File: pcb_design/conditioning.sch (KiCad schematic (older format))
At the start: 41 parts, among them U3 OPA2376AID, U4 LM2903-SO8

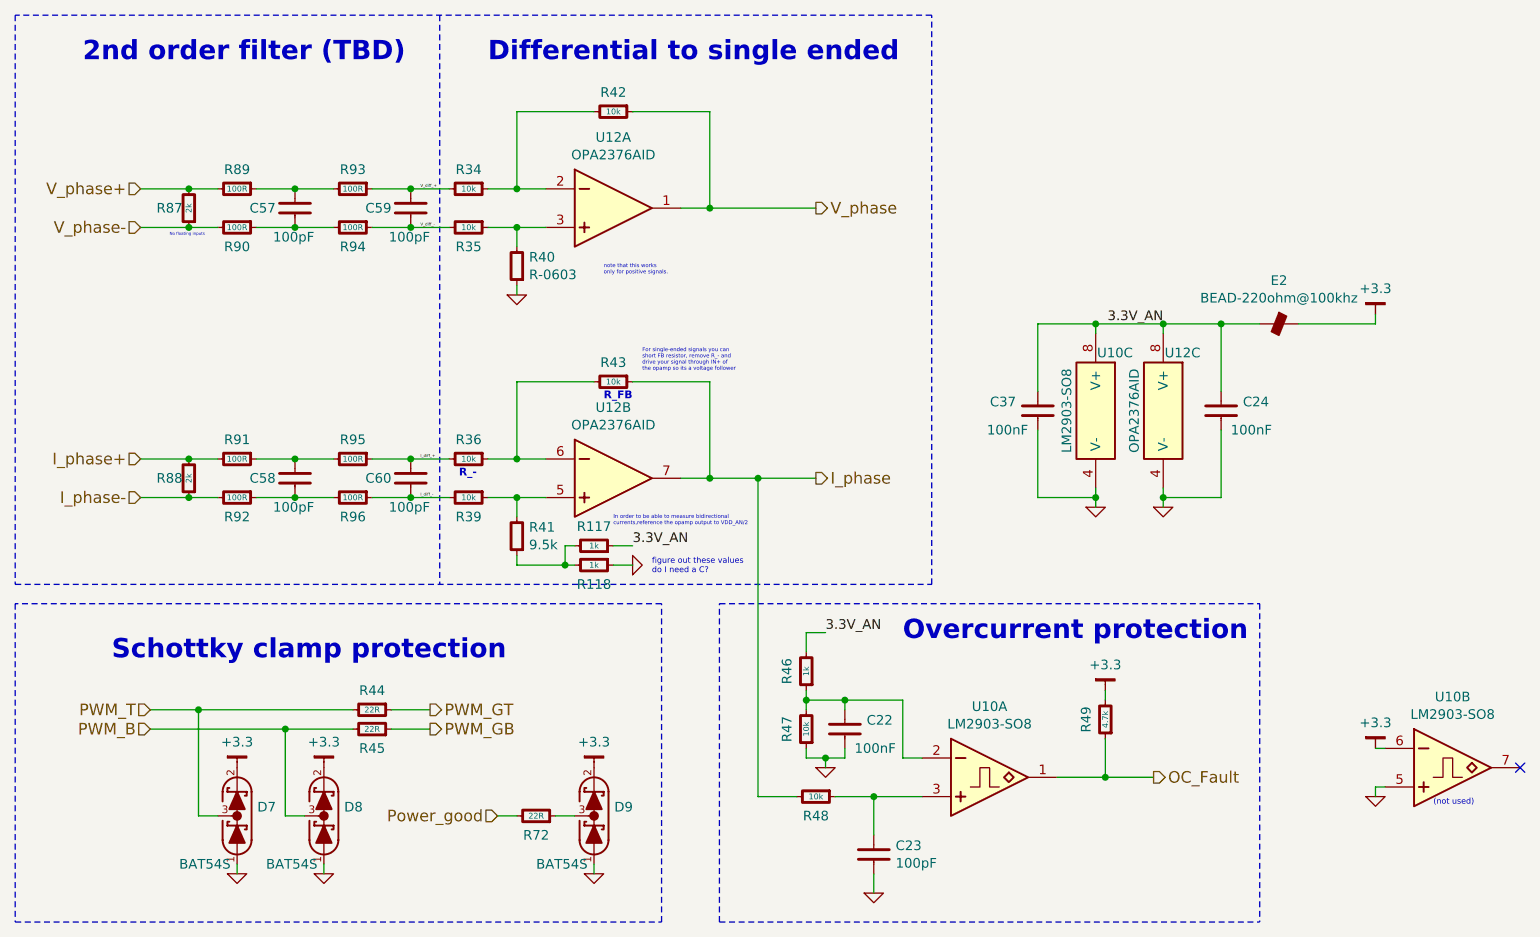
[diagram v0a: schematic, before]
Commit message: Added reverse polarity protection on the isolated side of CON connector. Also, more layout
Signed-off-by: Marcos Chaparro <mchaparro@paltatech.com>
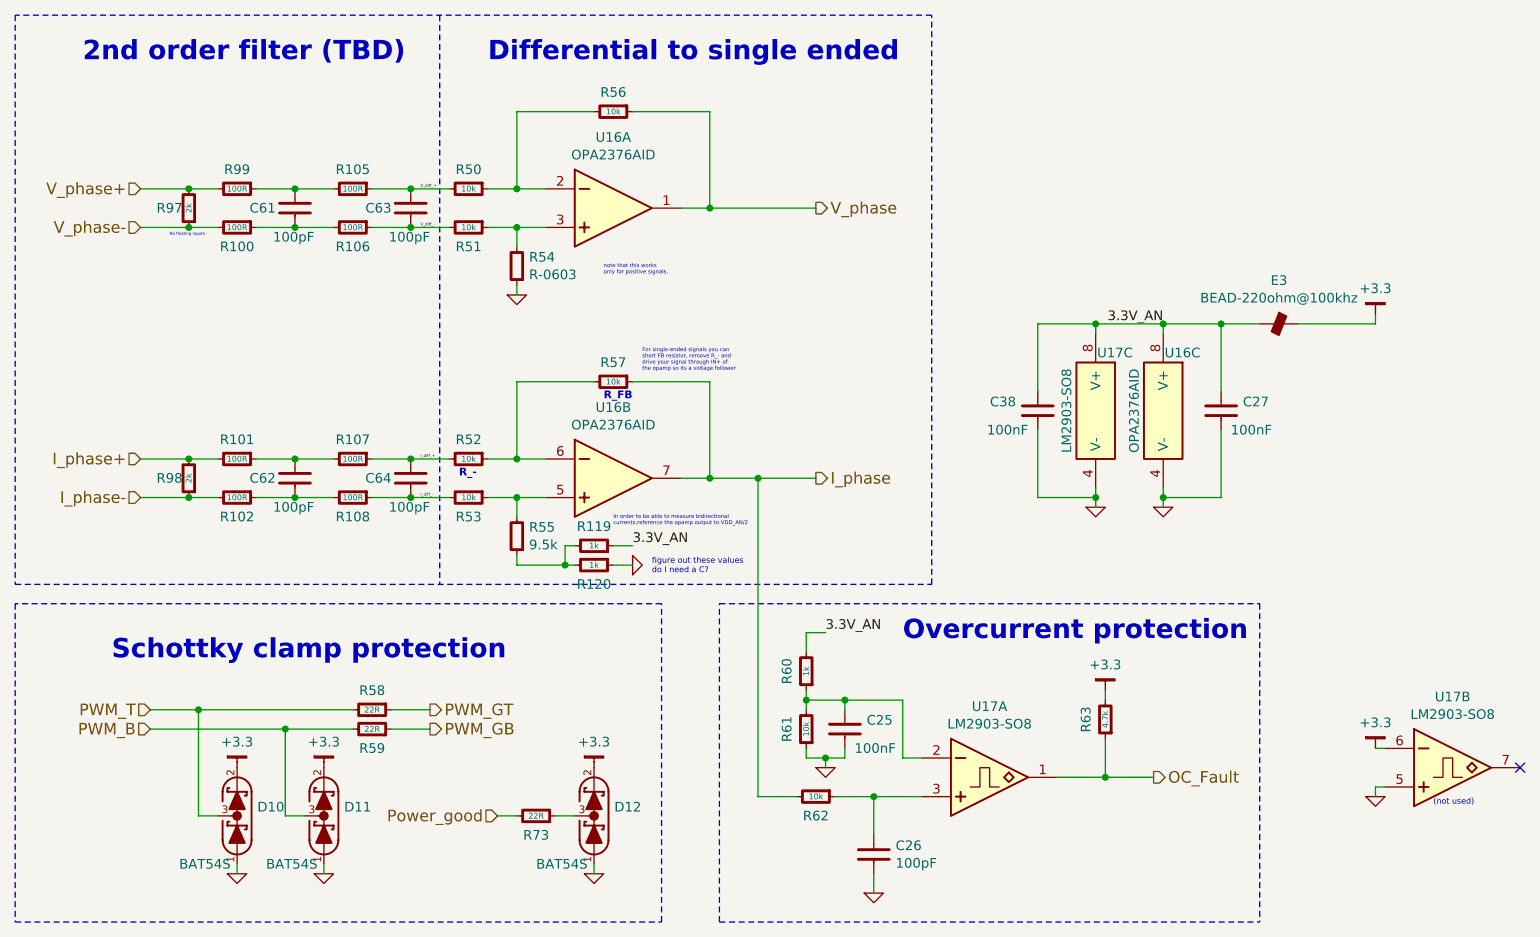
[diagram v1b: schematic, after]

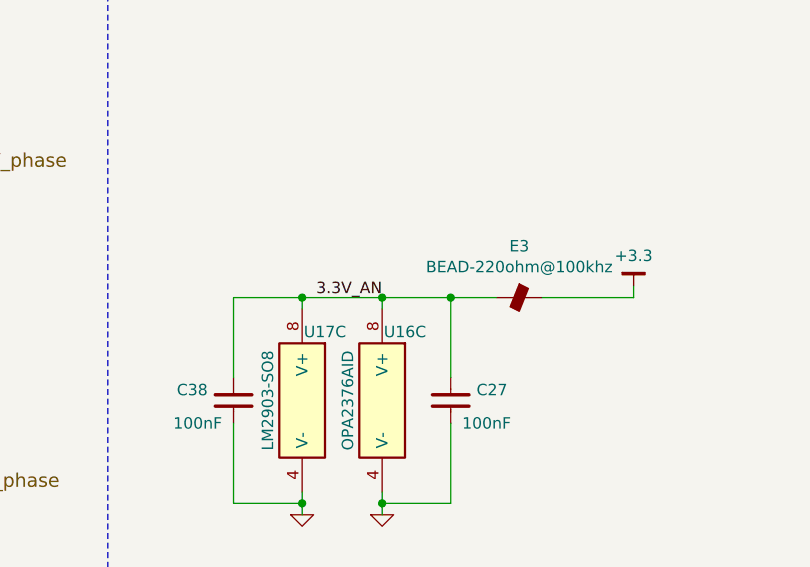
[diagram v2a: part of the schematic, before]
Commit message: Routing complete. Added 3D models. No DRC errors, a few ERC warnings
Signed-off-by: Marcos Chaparro <mchaparro@paltatech.com>
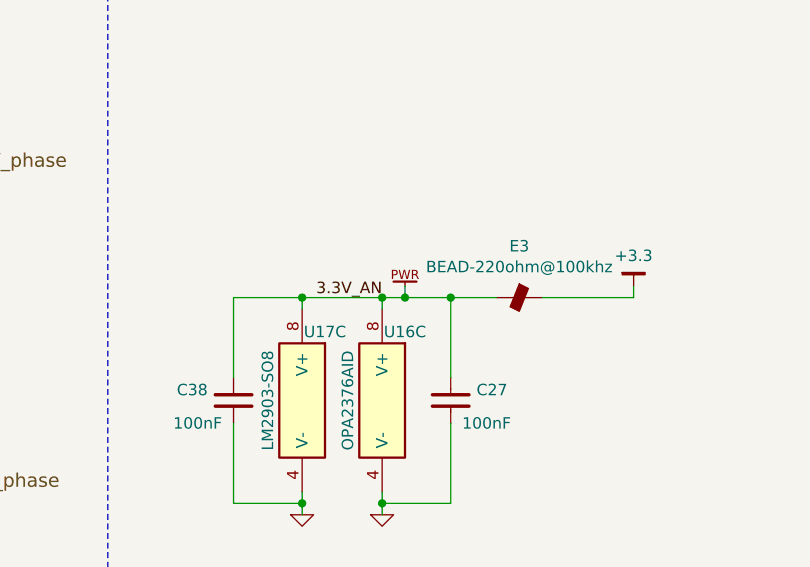
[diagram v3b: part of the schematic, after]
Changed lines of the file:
@@
 $EndComp
 $Comp
-L GND #PWR051
+L GND #PWR056
 U 1 1 588D9158
 P 5100 3000
-AR Path="/5886DA84/588D9158" Ref="#PWR051"  Part="1"
-AR Path="/588C2790/588D9158" Ref="#PWR0113"  Part="1"
-AR Path="/588C4E84/588D9158" Ref="#PWR0129"  Part="1"
-F 0 "#PWR0129" H 5100 3000 30  0001 C CNN
+AR Path="/5886DA84/588D9158" Ref="#PWR056"  Part="1"
+AR Path="/588C2790/588D9158" Ref="#PWR0125"  Part="1"
+AR Path="/588C4E84/588D9158" Ref="#PWR0142"  Part="1"
+F 0 "#PWR0142" H 5100 3000 30  0001 C CNN
 F 1 "GND" H 5100 2930 30  0001 C CNN
 F 2 "" H 5100 3000 60  0000 C CNN
@@
 $EndComp
 $Comp
-L GND #PWR052
+L GND #PWR057
 U 1 1 588D96F7
 P 5700 4400
-AR Path="/5886DA84/588D96F7" Ref="#PWR052"  Part="1"
-AR Path="/588C2790/588D96F7" Ref="#PWR0114"  Part="1"
-AR Path="/588C4E84/588D96F7" Ref="#PWR0130"  Part="1"
-F 0 "#PWR0130" H 5700 4400 30  0001 C CNN
+AR Path="/5886DA84/588D96F7" Ref="#PWR057"  Part="1"
+AR Path="/588C2790/588D96F7" Ref="#PWR0126"  Part="1"
+AR Path="/588C4E84/588D96F7" Ref="#PWR0143"  Part="1"
+F 0 "#PWR0143" H 5700 4400 30  0001 C CNN
 F 1 "GND" H 5700 4330 30  0001 C CNN
 F 2 "" H 5700 4400 60  0000 C CNN
@@
 $EndComp
 $Comp
-L GND #PWR053
+L GND #PWR058
 U 1 1 588DAB09
 P 6950 6100
-AR Path="/5886DA84/588DAB09" Ref="#PWR053"  Part="1"
-AR Path="/588C2790/588DAB09" Ref="#PWR0115"  Part="1"
-AR Path="/588C4E84/588DAB09" Ref="#PWR0131"  Part="1"
-F 0 "#PWR0131" H 6950 6100 30  0001 C CNN
+AR Path="/5886DA84/588DAB09" Ref="#PWR058"  Part="1"
+AR Path="/588C2790/588DAB09" Ref="#PWR0127"  Part="1"
+AR Path="/588C4E84/588DAB09" Ref="#PWR0144"  Part="1"
+F 0 "#PWR0144" H 6950 6100 30  0001 C CNN
 F 1 "GND" H 6950 6030 30  0001 C CNN
 F 2 "" H 6950 6100 60  0000 C CNN
@@
 $EndComp
 $Comp
-L GND #PWR054
+L GND #PWR059
 U 1 1 588DB3CB
 P 6700 5450
-AR Path="/5886DA84/588DB3CB" Ref="#PWR054"  Part="1"
-AR Path="/588C2790/588DB3CB" Ref="#PWR0116"  Part="1"
-AR Path="/588C4E84/588DB3CB" Ref="#PWR0132"  Part="1"
-F 0 "#PWR0132" H 6700 5450 30  0001 C CNN
+AR Path="/5886DA84/588DB3CB" Ref="#PWR059"  Part="1"
+AR Path="/588C2790/588DB3CB" Ref="#PWR0128"  Part="1"
+AR Path="/588C4E84/588DB3CB" Ref="#PWR0145"  Part="1"
+F 0 "#PWR0145" H 6700 5450 30  0001 C CNN
 F 1 "GND" H 6700 5380 30  0001 C CNN
 F 2 "" H 6700 5450 60  0000 C CNN
@@
 $EndComp
 $Comp
-L GND #PWR055
+L GND #PWR060
 U 1 1 588818FC
 P 8450 4100
-AR Path="/5886DA84/588818FC" Ref="#PWR055"  Part="1"
-AR Path="/588C2790/588818FC" Ref="#PWR0117"  Part="1"
-AR Path="/588C4E84/588818FC" Ref="#PWR0133"  Part="1"
-F 0 "#PWR0133" H 8450 4100 30  0001 C CNN
+AR Path="/5886DA84/588818FC" Ref="#PWR060"  Part="1"
+AR Path="/588C2790/588818FC" Ref="#PWR0129"  Part="1"
+AR Path="/588C4E84/588818FC" Ref="#PWR0146"  Part="1"
+F 0 "#PWR0146" H 8450 4100 30  0001 C CNN
 F 1 "GND" H 8450 4030 30  0001 C CNN
 F 2 "" H 8450 4100 60  0000 C CNN
@@
 $EndComp
 $Comp
-L GND #PWR056
+L GND #PWR061
 U 1 1 58891279
 P 3650 6000
-AR Path="/5886DA84/58891279" Ref="#PWR056"  Part="1"
-AR Path="/588C2790/58891279" Ref="#PWR0118"  Part="1"
-AR Path="/588C4E84/58891279" Ref="#PWR0134"  Part="1"
-F 0 "#PWR0134" H 3650 6000 30  0001 C CNN
+AR Path="/5886DA84/58891279" Ref="#PWR061"  Part="1"
+AR Path="/588C2790/58891279" Ref="#PWR0130"  Part="1"
+AR Path="/588C4E84/58891279" Ref="#PWR0147"  Part="1"
+F 0 "#PWR0147" H 3650 6000 30  0001 C CNN
 F 1 "GND" H 3650 5930 30  0001 C CNN
 F 2 "" H 3650 6000 60  0000 C CNN
@@
 $EndComp
 $Comp
-L GND #PWR057
+L GND #PWR062
 U 1 1 58891376
 P 4100 6000
-AR Path="/5886DA84/58891376" Ref="#PWR057"  Part="1"
-AR Path="/588C2790/58891376" Ref="#PWR0119"  Part="1"
-AR Path="/588C4E84/58891376" Ref="#PWR0135"  Part="1"
-F 0 "#PWR0135" H 4100 6000 30  0001 C CNN
+AR Path="/5886DA84/58891376" Ref="#PWR062"  Part="1"
+AR Path="/588C2790/58891376" Ref="#PWR0131"  Part="1"
+AR Path="/588C4E84/58891376" Ref="#PWR0148"  Part="1"
+F 0 "#PWR0148" H 4100 6000 30  0001 C CNN
 F 1 "GND" H 4100 5930 30  0001 C CNN
 F 2 "" H 4100 6000 60  0000 C CNN
@@
 $EndComp
 $Comp
-L GND #PWR058
+L GND #PWR063
 U 1 1 5889172A
 P 5500 6000
-AR Path="/5886DA84/5889172A" Ref="#PWR058"  Part="1"
-AR Path="/588C2790/5889172A" Ref="#PWR0120"  Part="1"
-AR Path="/588C4E84/5889172A" Ref="#PWR0136"  Part="1"
-F 0 "#PWR0136" H 5500 6000 30  0001 C CNN
+AR Path="/5886DA84/5889172A" Ref="#PWR063"  Part="1"
+AR Path="/588C2790/5889172A" Ref="#PWR0132"  Part="1"
+AR Path="/588C4E84/5889172A" Ref="#PWR0149"  Part="1"
+F 0 "#PWR0149" H 5500 6000 30  0001 C CNN
 F 1 "GND" H 5500 5930 30  0001 C CNN
 F 2 "" H 5500 6000 60  0000 C CNN
@@
 $EndComp
 $Comp
-L GND #PWR059
+L GND #PWR064
 U 1 1 58899625
 P 8100 4100
-AR Path="/5886DA84/58899625" Ref="#PWR059"  Part="1"
-AR Path="/588C2790/58899625" Ref="#PWR0121"  Part="1"
-AR Path="/588C4E84/58899625" Ref="#PWR0137"  Part="1"
-F 0 "#PWR0137" H 8100 4100 30  0001 C CNN
+AR Path="/5886DA84/58899625" Ref="#PWR064"  Part="1"
+AR Path="/588C2790/58899625" Ref="#PWR0133"  Part="1"
+AR Path="/588C4E84/58899625" Ref="#PWR0150"  Part="1"
+F 0 "#PWR0150" H 8100 4100 30  0001 C CNN
 F 1 "GND" H 8100 4030 30  0001 C CNN
 F 2 "" H 8100 4100 60  0000 C CNN
@@
 2nd order filter (TBD)
 $Comp
-L +3.3 #PWR060
+L +3.3 #PWR065
 U 1 1 588B58C9
 P 9550 3100
-AR Path="/5886DA84/588B58C9" Ref="#PWR060"  Part="1"
-AR Path="/588C2790/588B58C9" Ref="#PWR0122"  Part="1"
-AR Path="/588C4E84/588B58C9" Ref="#PWR0138"  Part="1"
-F 0 "#PWR0138" H 9600 3150 30  0001 C CNN
+AR Path="/5886DA84/588B58C9" Ref="#PWR065"  Part="1"
+AR Path="/588C2790/588B58C9" Ref="#PWR0134"  Part="1"
+AR Path="/588C4E84/588B58C9" Ref="#PWR0151"  Part="1"
+F 0 "#PWR0151" H 9600 3150 30  0001 C CNN
 F 1 "+3.3" H 9550 3233 50  0000 C CNN
 F 2 "" H 300 -50 60  0000 C CNN
@@
 $EndComp
 $Comp
-L +3.3 #PWR061
+L +3.3 #PWR066
 U 1 1 588B5AA1
 P 8150 5050
-AR Path="/5886DA84/588B5AA1" Ref="#PWR061"  Part="1"
-AR Path="/588C2790/588B5AA1" Ref="#PWR0123"  Part="1"
-AR Path="/588C4E84/588B5AA1" Ref="#PWR0139"  Part="1"
-F 0 "#PWR0139" H 8200 5100 30  0001 C CNN
+AR Path="/5886DA84/588B5AA1" Ref="#PWR066"  Part="1"
+AR Path="/588C2790/588B5AA1" Ref="#PWR0135"  Part="1"
+AR Path="/588C4E84/588B5AA1" Ref="#PWR0152"  Part="1"
+F 0 "#PWR0152" H 8200 5100 30  0001 C CNN
 F 1 "+3.3" H 8150 5183 50  0000 C CNN
 F 2 "" H 300 -50 60  0000 C CNN
@@
 $EndComp
 $Comp
-L +3.3 #PWR062
+L +3.3 #PWR067
 U 1 1 588B5C24
 P 5500 5450
-AR Path="/5886DA84/588B5C24" Ref="#PWR062"  Part="1"
-AR Path="/588C2790/588B5C24" Ref="#PWR0124"  Part="1"
-AR Path="/588C4E84/588B5C24" Ref="#PWR0140"  Part="1"
-F 0 "#PWR0140" H 5550 5500 30  0001 C CNN
+AR Path="/5886DA84/588B5C24" Ref="#PWR067"  Part="1"
+AR Path="/588C2790/588B5C24" Ref="#PWR0136"  Part="1"
+AR Path="/588C4E84/588B5C24" Ref="#PWR0153"  Part="1"
+F 0 "#PWR0153" H 5550 5500 30  0001 C CNN
 F 1 "+3.3" H 5500 5583 50  0000 C CNN
 F 2 "" H -2350 350 60  0000 C CNN
@@
 $EndComp
 $Comp
-L +3.3 #PWR063
+L +3.3 #PWR068
 U 1 1 588B5D7A
 P 3650 5450
-AR Path="/5886DA84/588B5D7A" Ref="#PWR063"  Part="1"
-AR Path="/588C2790/588B5D7A" Ref="#PWR0125"  Part="1"
-AR Path="/588C4E84/588B5D7A" Ref="#PWR0141"  Part="1"
-F 0 "#PWR0141" H 3700 5500 30  0001 C CNN
+AR Path="/5886DA84/588B5D7A" Ref="#PWR068"  Part="1"
+AR Path="/588C2790/588B5D7A" Ref="#PWR0137"  Part="1"
+AR Path="/588C4E84/588B5D7A" Ref="#PWR0154"  Part="1"
+F 0 "#PWR0154" H 3700 5500 30  0001 C CNN
 F 1 "+3.3" H 3650 5583 50  0000 C CNN
 F 2 "" H -4200 350 60  0000 C CNN
@@
 $EndComp
 $Comp
-L +3.3 #PWR064
+L +3.3 #PWR069
 U 1 1 588B5E7B
 P 4100 5450
-AR Path="/5886DA84/588B5E7B" Ref="#PWR064"  Part="1"
-AR Path="/588C2790/588B5E7B" Ref="#PWR0126"  Part="1"
-AR Path="/588C4E84/588B5E7B" Ref="#PWR0142"  Part="1"
-F 0 "#PWR0142" H 4150 5500 30  0001 C CNN
+AR Path="/5886DA84/588B5E7B" Ref="#PWR069"  Part="1"
+AR Path="/588C2790/588B5E7B" Ref="#PWR0138"  Part="1"
+AR Path="/588C4E84/588B5E7B" Ref="#PWR0155"  Part="1"
+F 0 "#PWR0155" H 4150 5500 30  0001 C CNN
 F 1 "+3.3" H 4100 5583 50  0000 C CNN
 F 2 "" H -3750 350 60  0000 C CNN
@@
 No floating inputs
 $Comp
-L GND #PWR0127
+L GND #PWR0139
 U 1 1 588CC75B
 P 9550 5600
-AR Path="/588C2790/588CC75B" Ref="#PWR0127"  Part="1"
-AR Path="/5886DA84/588CC75B" Ref="#PWR065"  Part="1"
-AR Path="/588C4E84/588CC75B" Ref="#PWR0143"  Part="1"
-F 0 "#PWR0143" H 9600 5650 30  0001 C CNN
+AR Path="/588C2790/588CC75B" Ref="#PWR0139"  Part="1"
+AR Path="/5886DA84/588CC75B" Ref="#PWR070"  Part="1"
+AR Path="/588C4E84/588CC75B" Ref="#PWR0156"  Part="1"
+F 0 "#PWR0156" H 9600 5650 30  0001 C CNN
 F 1 "GND" H 300 -20 30  0001 C CNN
 F 2 "" H 300 50  60  0000 C CNN
@@
 $EndComp
 $Comp
-L +3.3 #PWR066
+L +3.3 #PWR071
 U 1 1 588CC994
 P 9550 5350
-AR Path="/5886DA84/588CC994" Ref="#PWR066"  Part="1"
-AR Path="/588C2790/588CC994" Ref="#PWR0128"  Part="1"
-AR Path="/588C4E84/588CC994" Ref="#PWR0144"  Part="1"
-F 0 "#PWR0144" H 9600 5400 30  0001 C CNN
+AR Path="/5886DA84/588CC994" Ref="#PWR071"  Part="1"
+AR Path="/588C2790/588CC994" Ref="#PWR0140"  Part="1"
+AR Path="/588C4E84/588CC994" Ref="#PWR0157"  Part="1"
+F 0 "#PWR0157" H 9600 5400 30  0001 C CNN
 F 1 "+3.3" H 9550 5483 50  0000 C CNN
 F 2 "" H 1700 250 60  0000 C CNN
@@
 	5100 4400 5400 4400
 Connection ~ 5350 4400
+$Comp
+L PWR_FLAG #PWR072
+U 1 1 5893CFA6
+P 8550 3100
+AR Path="/5886DA84/5893CFA6" Ref="#PWR072"  Part="1"
+AR Path="/588C2790/5893CFA6" Ref="#PWR0141"  Part="1"
+AR Path="/588C4E84/5893CFA6" Ref="#PWR0158"  Part="1"
+F 0 "#PWR0158" H 8600 3150 50  0001 C CNN
+F 1 "PWR_FLAG" H 150 500 50  0001 C CNN
+F 2 "" H 150 500 60  0000 C CNN
+F 3 "" H 150 500 60  0000 C CNN
+	1    8550 3100
+	1    0    0    -1
+$EndComp
+Wire Wire Line
+	8550 3100 8550 3150
+Connection ~ 8550 3150
 $EndSCHEMATC
